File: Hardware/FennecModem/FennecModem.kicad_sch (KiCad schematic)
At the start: 19 parts, among them J101 USB_C_Receptacle_USB2.0, J102 ICSP, SW101 RESET, U101 ATmega32U4-A, Y101 16mHz

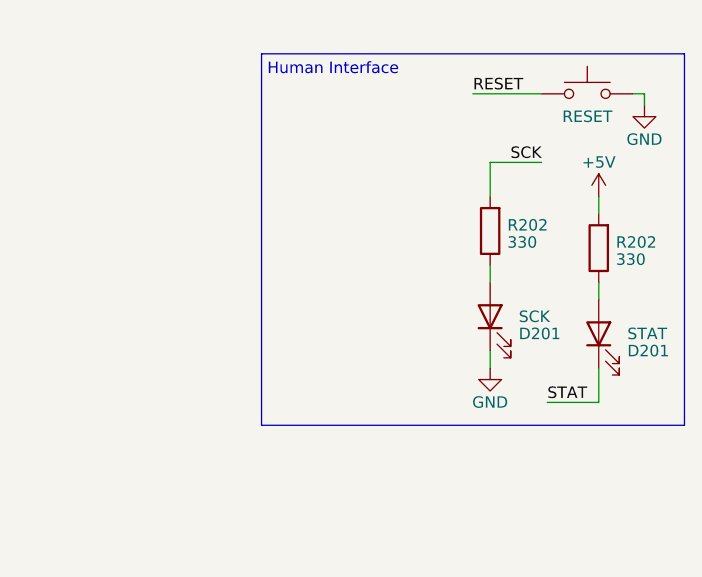
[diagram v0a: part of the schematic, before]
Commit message: Bump rails and add PWR LED
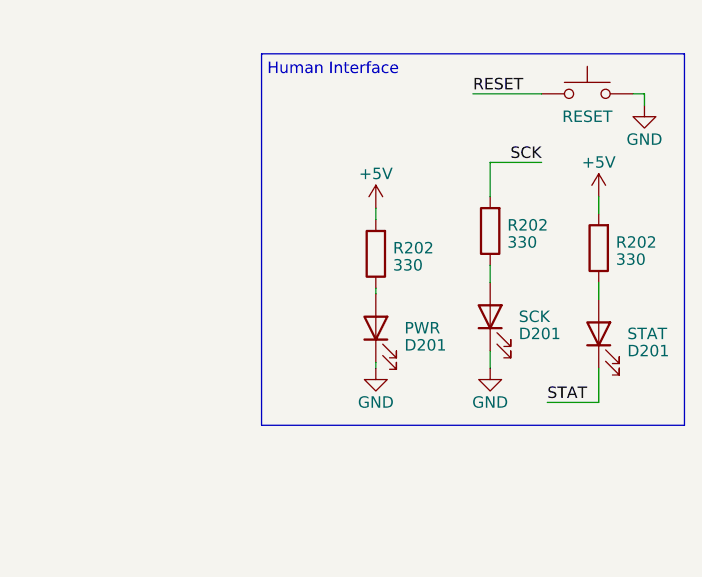
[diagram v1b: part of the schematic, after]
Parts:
- added D201: PWR, LED_THT:LED_D3.0mm_Horizontal_O1.27mm_Z2.0mm, symbol Device:LED
- added R202: 330, Resistor_SMD:R_0805_2012Metric, symbol Device:R
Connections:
- net +5V: now also R202.2
- net GND: now also D201.1 (K)
- new net: D201.2 (A), R202.1
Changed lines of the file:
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@@
+    (stroke (width 0) (type default))
+  )
+  (wire (pts (xy 250.19 140.97) (xy 250.19 142.24))
     (stroke (width 0) (type default))
   )
@@
     (stroke (width 0) (type default))
   )
+  (wire (pts (xy 250.19 149.86) (xy 250.19 150.495))
+    (stroke (width 0) (type default))
+  )
   (wire (pts (xy 93.98 90.805) (xy 105.41 90.805))
     (stroke (width 0) (type default))
@@
   )
   (wire (pts (xy 22.225 190.5) (xy 26.035 190.5))
+    (stroke (width 0) (type default))
+  )
+  (wire (pts (xy 250.19 158.115) (xy 250.19 158.75))
     (stroke (width 0) (type default))
   )
@@
     )
   )
+  (symbol (lib_id "power:GND") (at 250.19 158.75 0) (unit 1)
+    (in_bom yes) (on_board yes) (dnp no)
+    (property "Reference" "#PWR0116" (at 250.19 165.1 0)
+      (effects (font (size 1.27 1.27)) hide)
+    )
+    (property "Value" "GND" (at 250.19 162.56 0)
+      (effects (font (size 1.27 1.27)))
+    )
+    (property "Footprint" "" (at 250.19 158.75 0)
+      (effects (font (size 1.27 1.27)) hide)
+    )
+    (property "Datasheet" "" (at 250.19 158.75 0)
+      (effects (font (size 1.27 1.27)) hide)
+    )
+    (pin "1")
+    (instances
+      (project "FennecModem"
+        (path "/8cb1f8f8-0f28-4c6f-8a0b-e6b064917aa9"
+          (reference "#PWR0116") (unit 1)
+        )
+      )
+      (project "Segment_Display_Board"
+        (path "/b2a59c5b-d3e3-43eb-8828-f00d6845168f/5b3b94e9-8561-416b-92c8-c061c8d10891"
+          (reference "#PWR0218") (unit 1)
+        )
+      )
+    )
+  )
   (symbol (lib_id "power:GND") (at 105.41 119.38 0) (unit 1)
     (in_bom yes) (on_board yes) (dnp no)
@@
         (path "/e51b0d47-7e88-4bbf-adc2-21abe8ab62c1"
           (reference "#PWR0115") (unit 1)
+        )
+      )
+    )
+  )
+  (symbol (lib_id "Device:R") (at 250.19 146.05 180) (unit 1)
+    (in_bom yes) (on_board yes) (dnp no)
+    (property "Reference" "R202" (at 252.095 145.415 0)
+      (effects (font (size 1.27 1.27)) (justify right))
+    )
+    (property "Value" "330" (at 252.095 147.32 0)
+      (effects (font (size 1.27 1.27)) (justify right))
+    )
+    (property "Footprint" "Resistor_SMD:R_0805_2012Metric" (at 251.968 146.05 90)
+      (effects (font (size 1.27 1.27)) hide)
+    )
+    (property "Datasheet" "~" (at 250.19 146.05 0)
+      (effects (font (size 1.27 1.27)) hide)
+    )
+    (pin "1")
+    (pin "2")
+    (instances
+      (project "FennecModem"
+        (path "/8cb1f8f8-0f28-4c6f-8a0b-e6b064917aa9/cf3d0f33-271b-4df1-9d86-6d97bc01010a"
+          (reference "R202") (unit 1)
+        )
+        (path "/8cb1f8f8-0f28-4c6f-8a0b-e6b064917aa9"
+          (reference "R108") (unit 1)
         )
       )
@@
     )
   )
+  (symbol (lib_id "Device:LED") (at 250.19 154.305 90) (unit 1)
+    (in_bom yes) (on_board yes) (dnp no)
+    (property "Reference" "D201" (at 253.365 156.21 90)
+      (effects (font (size 1.27 1.27)) (justify right))
+    )
+    (property "Value" "PWR" (at 253.365 154.305 90)
+      (effects (font (size 1.27 1.27)) (justify right))
+    )
+    (property "Footprint" "LED_THT:LED_D3.0mm_Horizontal_O1.27mm_Z2.0mm" (at 250.19 154.305 0)
+      (effects (font (size 1.27 1.27)) hide)
+    )
+    (property "Datasheet" "~" (at 250.19 154.305 0)
+      (effects (font (size 1.27 1.27)) hide)
+    )
+    (pin "1")
+    (pin "2")
+    (instances
+      (project "FennecModem"
+        (path "/8cb1f8f8-0f28-4c6f-8a0b-e6b064917aa9/cf3d0f33-271b-4df1-9d86-6d97bc01010a"
+          (reference "D201") (unit 1)
+        )
+        (path "/8cb1f8f8-0f28-4c6f-8a0b-e6b064917aa9"
+          (reference "D104") (unit 1)
+        )
+      )
+    )
+  )
   (symbol (lib_id "power:GND") (at 95.885 73.025 0) (unit 1)
     (in_bom yes) (on_board yes) (dnp no)
@@
         )
       )
+    )
+  )
+  (symbol (lib_id "power:+5V") (at 250.19 140.97 0) (unit 1)
+    (in_bom yes) (on_board yes) (dnp no)
+    (property "Reference" "#PWR0112" (at 250.19 144.78 0)
+      (effects (font (size 1.27 1.27)) hide)
+    )
+    (property "Value" "+5V" (at 250.19 137.16 0)
+      (effects (font (size 1.27 1.27)))
+    )
+    (property "Footprint" "" (at 250.19 140.97 0)
+      (effects (font (size 1.27 1.27)) hide)
+    )
+    (property "Datasheet" "" (at 250.19 140.97 0)
+      (effects (font (size 1.27 1.27)) hide)
+    )
+    (pin "1")
+    (instances
+      (project "FennecModem"
+        (path "/8cb1f8f8-0f28-4c6f-8a0b-e6b064917aa9/cf3d0f33-271b-4df1-9d86-6d97bc01010a"
+          (reference "#PWR0112") (unit 1)
+        )
+        (path "/8cb1f8f8-0f28-4c6f-8a0b-e6b064917aa9"
+          (reference "#PWR0117") (unit 1)
+        )
+      )

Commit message: Bump backplane
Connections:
- net I2C_CLK: now also U101.18 (PD0)
- net I2C_SDA: now also U101.19 (PD1)
- net RXD: now reaches U101.20 (PD2)
- net TXD: now reaches U101.21 (PD3)
- net TX_SIGNAL: now reaches U101.30 (PB6)
- net RX_SIGNAL: now reaches U101.41 (PF0)
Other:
- note added: "PB6/ADC13 Should be able to handle 16bit pwm"
- note added: "PF0 or A5 is ADC0"
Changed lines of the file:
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@@
+    (stroke (width 0) (type default))
+  )
+  (wire (pts (xy 249.555 83.82) (xy 252.73 83.82))
     (stroke (width 0) (type default))
   )
@@
     (stroke (width 0) (type default))
   )
+  (wire (pts (xy 249.555 85.725) (xy 252.73 85.725))
+    (stroke (width 0) (type default))
+  )
   (wire (pts (xy 123.19 67.945) (xy 114.3 67.945))
     (stroke (width 0) (type default))
@@
     (stroke (width 0) (type default))
   )
-  (wire (pts (xy 163.195 65.405) (xy 153.67 65.405))
+  (wire (pts (xy 167.005 65.405) (xy 153.67 65.405))
     (stroke (width 0) (type default))
   )
@@
     (stroke (width 0) (type default))
   )
+  (wire (pts (xy 242.57 83.82) (xy 247.65 83.82))
+    (stroke (width 0) (type default))
+  )
   (wire (pts (xy 262.89 158.75) (xy 262.89 156.845))
     (stroke (width 0) (type default))
@@
     (stroke (width 0) (type default))
   )
+  (wire (pts (xy 242.57 85.725) (xy 247.65 85.725))
+    (stroke (width 0) (type default))
+  )
+  (wire (pts (xy 167.64 93.345) (xy 153.67 93.345))
+    (stroke (width 0) (type default))
+  )
   (wire (pts (xy 114.3 73.025) (xy 123.19 73.025))
     (stroke (width 0) (type default))
@@
     (stroke (width 0) (type default))
   )
+  (wire (pts (xy 167.64 98.425) (xy 153.67 98.425))
+    (stroke (width 0) (type default))
+  )
   (wire (pts (xy 41.275 168.275) (xy 48.26 168.275))
     (stroke (width 0) (type default))
@@
     (stroke (width 0) (type default))
   )
+  (wire (pts (xy 153.67 123.825) (xy 167.64 123.825))
+    (stroke (width 0) (type default))
+  )
   (wire (pts (xy 138.43 52.705) (xy 140.97 52.705))
     (stroke (width 0) (type default))
@@
     (stroke (width 0) (type default))
   )
+  (wire (pts (xy 167.64 100.965) (xy 153.67 100.965))
+    (stroke (width 0) (type default))
+  )
   (wire (pts (xy 120.65 62.865) (xy 123.19 62.865))
     (stroke (width 0) (type default))
@@
     (stroke (width 0) (type default))
   )
-  (wire (pts (xy 163.195 67.945) (xy 153.67 67.945))
+  (wire (pts (xy 167.005 67.945) (xy 153.67 67.945))
     (stroke (width 0) (type default))
   )
@@
     (stroke (width 0) (type default))
   )
+  (wire (pts (xy 247.65 85.725) (xy 249.555 83.82))
+    (stroke (width 0) (type default))
+  )
   (wire (pts (xy 22.225 190.5) (xy 26.035 190.5))
     (stroke (width 0) (type default))
@@
     (stroke (width 0) (type default))
   )
-  (wire (pts (xy 163.195 70.485) (xy 153.67 70.485))
+  (wire (pts (xy 247.65 83.82) (xy 249.555 85.725))
+    (stroke (width 0) (type default))
+  )
+  (wire (pts (xy 167.005 70.485) (xy 153.67 70.485))
+    (stroke (width 0) (type default))
+  )
+  (wire (pts (xy 167.64 95.885) (xy 153.67 95.885))
     (stroke (width 0) (type default))
   )
@@
     (stroke (width 0) (type default))
   )
+  (wire (pts (xy 153.67 78.105) (xy 167.64 78.105))
+    (stroke (width 0) (type default))
+  )
   (polyline (pts (xy 175.895 196.85) (xy 175.895 173.99))
     (stroke (width 0) (type default))
+  )
+  (text "PF0 or A5 is ADC0" (at 168.91 123.825 0)
+    (effects (font (size 1.27 1.27)) (justify left bottom))
+  )
+  (text "PB6/ADC13\nShould be able to handle\n16bit pwm" (at 168.91 80.645 0)
+    (effects (font (size 1.27 1.27)) (justify left bottom))
   )
   (text "Human Interface" (at 238.125 126.365 0)
@@
     (effects (font (size 1.27 1.27)) (justify left bottom))
   )
+  (label "RXD" (at 242.57 83.82 0) (fields_autoplaced)
+    (effects (font (size 1.27 1.27)) (justify left bottom))
+  )
+  (label "TX_SIGNAL" (at 167.64 78.105 180) (fields_autoplaced)
+    (effects (font (size 1.27 1.27)) (justify right bottom))
+  )
   (label "RESET" (at 145.415 188.595 0) (fields_autoplaced)
     (effects (font (size 1.27 1.27)) (justify left bottom))
   )
-  (label "SDO" (at 163.195 67.945 180) (fields_autoplaced)
+  (label "RXD" (at 167.64 98.425 180) (fields_autoplaced)
+    (effects (font (size 1.27 1.27)) (justify right bottom))
+  )
+  (label "SDO" (at 167.005 67.945 180) (fields_autoplaced)
     (effects (font (size 1.27 1.27)) (justify right bottom))
   )
@@
     (effects (font (size 1.27 1.27)) (justify right bottom))
   )
-  (label "I2C_CLK" (at 167.64 74.295 0) (fields_autoplaced)
-    (effects (font (size 1.27 1.27)) (justify left bottom))
+  (label "I2C_CLK" (at 167.64 93.345 180) (fields_autoplaced)
+    (effects (font (size 1.27 1.27)) (justify right bottom))
   )
   (label "SDO" (at 173.355 186.055 180) (fields_autoplaced)
@@
     (effects (font (size 1.27 1.27)) (justify left bottom))
   )
+  (label "TXD" (at 167.64 100.965 180) (fields_autoplaced)
+    (effects (font (size 1.27 1.27)) (justify right bottom))
+  )
+  (label "TXD" (at 242.57 85.725 0) (fields_autoplaced)
+    (effects (font (size 1.27 1.27)) (justify left bottom))
+  )
   (label "USB-" (at 93.98 90.805 0) (fields_autoplaced)
     (effects (font (size 1.27 1.27)) (justify left bottom))
@@
     (effects (font (size 1.27 1.27)) (justify left bottom))
   )
+  (label "RX_SIGNAL" (at 167.64 123.825 180) (fields_autoplaced)
+    (effects (font (size 1.27 1.27)) (justify right bottom))
+  )
   (label "RESET" (at 111.76 62.865 0) (fields_autoplaced)
     (effects (font (size 1.27 1.27)) (justify left bottom))
   )
-  (label "SCK" (at 163.195 65.405 180) (fields_autoplaced)
+  (label "SCK" (at 167.005 65.405 180) (fields_autoplaced)
     (effects (font (size 1.27 1.27)) (justify right bottom))
   )
@@
     (effects (font (size 1.27 1.27)) (justify left bottom))
   )
-  (label "SDI" (at 163.195 70.485 180) (fields_autoplaced)
+  (label "SDI" (at 167.005 70.485 180) (fields_autoplaced)
     (effects (font (size 1.27 1.27)) (justify right bottom))
   )
@@
     (effects (font (size 1.27 1.27)) (justify left bottom))
   )
-  (label "I2C_SDA" (at 167.64 79.375 0) (fields_autoplaced)
-    (effects (font (size 1.27 1.27)) (justify left bottom))
+  (label "I2C_SDA" (at 167.64 95.885 180) (fields_autoplaced)
+    (effects (font (size 1.27 1.27)) (justify right bottom))
   )
   (symbol (lib_id "Connector_Generic:Conn_02x03_Odd_Even") (at 158.75 186.055 0) (unit 1)
@@
     )
   )
-  (sheet (at 194.31 64.77) (size 24.765 24.13) (fields_autoplaced)
+  (sheet (at 252.73 64.77) (size 24.765 24.13) (fields_autoplaced)
     (stroke (width 0.1524) (type solid))
     (fill (color 0 0 0 0.0000))
-    (property "Sheetname" "Radio" (at 194.31 64.0584 0)
+    (property "Sheetname" "Radio" (at 252.73 64.0584 0)
       (effects (font (size 1.27 1.27)) (justify left bottom))
     )
-    (property "Sheetfile" "radio.kicad_sch" (at 194.31 89.4846 0)
+    (property "Sheetfile" "radio.kicad_sch" (at 252.73 89.4846 0)
       (effects (font (size 1.27 1.27)) (justify left top))
     )
-    (pin "AudioOut" output (at 194.31 67.945 180)
-      (effects (font (size 1.27 1.27)) (justify left))
-    )
-    (pin "AudioIn" input (at 194.31 69.85 180)
-      (effects (font (size 1.27 1.27)) (justify left))
-    )
-    (pin "PTT" input (at 194.31 74.295 180)
-      (effects (font (size 1.27 1.27)) (justify left))
-    )
-    (pin "TXD" output (at 194.31 85.725 180)
-      (effects (font (size 1.27 1.27)) (justify left))
-    )
-    (pin "RXD" input (at 194.31 83.82 180)
-      (effects (font (size 1.27 1.27)) (justify left))
-    )
-    (pin "Sleep" input (at 194.31 78.105 180)
-      (effects (font (size 1.27 1.27)) (justify left))
-    )
-    (pin "H{slash}L" input (at 194.31 76.2 180)
-      (effects (font (size 1.27 1.27)) (justify left))
-    )
-    (pin "SQL" output (at 194.31 80.01 180)
-      (effects (font (size 1.27 1.27)) (justify left))
-    )
+    (pin "AudioOut" output (at 252.73 67.945 180)
+      (effects (font (size 1.27 1.27)) (justify left))
+    )
+    (pin "AudioIn" input (at 252.73 69.85 180)
+      (effects (font (size 1.27 1.27)) (justify left))
+    )
+    (pin "PTT" input (at 252.73 74.295 180)
+      (effects (font (size 1.27 1.27)) (justify left))
+    )
+    (pin "TXD" output (at 252.73 85.725 180)
+      (effects (font (size 1.27 1.27)) (justify left))
+    )
+    (pin "RXD" input (at 252.73 83.82 180)
+      (effects (font (size 1.27 1.27)) (justify left))
+    )
+    (pin "Sleep" input (at 252.73 78.105 180)
+      (effects (font (size 1.27 1.27)) (justify left))
+    )
+    (pin "H{slash}L" input (at 252.73 76.2 180)
+      (effects (font (size 1.27 1.27)) (justify left))
+    )
+    (pin "SQL" output (at 252.73 80.01 180)
+      (effects (font (size 1.27 1.27)) (justify left))
+    )

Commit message: Add all
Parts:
- added D6: PRTR5V0U2X, Package_TO_SOT_SMD:SOT-143, symbol Power_Protection:PRTR5V0U2X
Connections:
- net +5V: now also D6.4 (VCC); no longer D105.1 (K)
- net GND: now also D6.1 (GND)
- net USB+: now also D6.2 (I/O1)
- net USB-: now also D6.3 (I/O2)
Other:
- moved on the sheet: R104, R105

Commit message: Include new chip! 3v3 system from now on..
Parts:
- removed U101: ATmega32U4-A, Package_QFP:TQFP-44_10x10mm_P0.8mm, symbol MCU_Microchip_ATmega:ATmega32U4-A
- added C101, C106, C107, C108, C109, C110, C111, C114, C115: 100nf, Capacitor_SMD:C_0805_2012Metric, symbol Device:C_Small
- added C112, C113: 1u, Capacitor_SMD:C_0805_2012Metric, symbol Device:C_Small
- added TP101: 1v1, TestPoint:TestPoint_Pad_D2.0mm, symbol Connector:TestPoint
- added U101: RP2040, Package_DFN_QFN:QFN-56-1EP_7x7mm_P0.4mm_EP3.2x3.2mm, symbol MCU_RaspberryPi:RP2040
- renumbered D201 to D101, D201 to D102, D201 to D104, R205 to R101, R205 to R102, R202 to R103, R205 to R106, R202 to R107, R202 to R108
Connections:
- net GND: now also C101.2, C106.2, C107.2, C108.2, C109.2, C110.2, C111.2, C112.2, C113.2, U101.57 (GND)
- new net: C114.2, C115.2
- new net +1V1: C113.1, C114.1, C115.1, TP101.1, U101.23 (DVDD), U101.45 (VREG_VOUT), U101.50 (DVDD)
- new net +3V3: C101.1, C106.1, C107.1, C108.1, C109.1, C110.1, C111.1, C112.1, U101.1 (IOVDD), U101.10 (IOVDD), U101.22 (IOVDD), U101.33 (IOVDD), U101.42 (IOVDD), U101.43 (ADC_AVDD), U101.44 (VREG_IN), U101.48 (USB_VDD), U101.49 (IOVDD)
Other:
- sheet Backplane ports: added SPI_CLK, SPI_SDA1, SPI_SDA2, SPI_SDA3, SPI_SDA4; removed none
- moved on the sheet: C102, C103, C104, C105, R101, R102, R106, Y101
